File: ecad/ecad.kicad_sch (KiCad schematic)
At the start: 79 parts, among them J1 JTAG, J2 USB_C, SW1 Kailh choc v2, SW10 RotaryEncoder_Switch, SW11 RotaryEncoder_Switch, SW12 Kailh choc v2, SW13 Kailh choc v2, SW14 Kailh choc v2, SW15 RESET, SW16 Kailh choc v2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

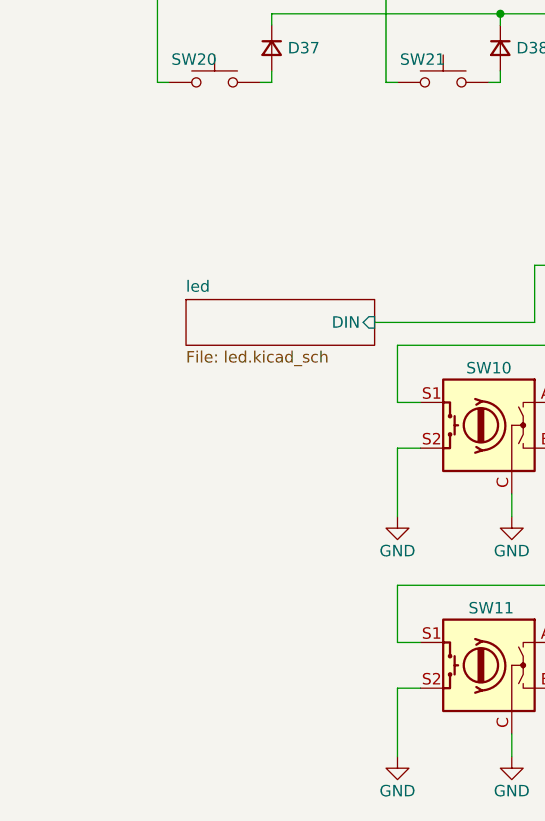
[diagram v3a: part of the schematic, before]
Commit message: feat(ecad): add buttons, fpc connector, and holes to pass flexible pcb of display
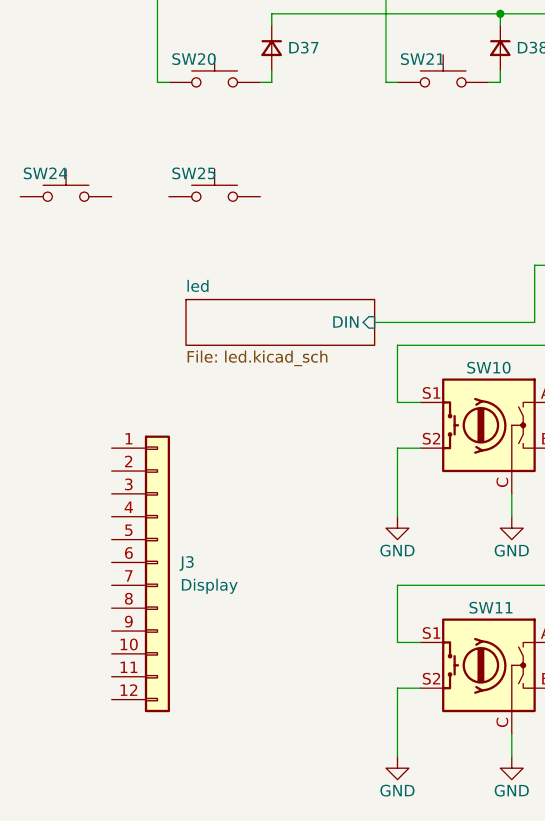
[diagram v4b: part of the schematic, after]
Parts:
- added J3: Display, Connector_FFC-FPC:Hirose_FH12-12S-0.5SH_1x12-1MP_P0.50mm_Horizontal, symbol Connector_Generic:Conn_01x12
- added SW24, SW25: Kailh choc v2, Button_Switch_THT:SW_PUSH_6mm, symbol Switch:SW_Push
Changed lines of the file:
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@@
+	)
+	(symbol
+		(lib_id "Switch:SW_Push")
+		(at 24.13 129.54 0)
+		(unit 1)
+		(exclude_from_sim no)
+		(in_bom yes)
+		(on_board yes)
+		(dnp no)
+		(property "Reference" "SW24"
+			(at 21.844 127 0)
+			(effects
+				(font
+					(size 1.27 1.27)
+				)
+			)
+		)
+		(property "Value" "Kailh choc v2"
+			(at 18.796 127 0)
+			(effects
+				(font
+					(size 1.27 1.27)
+				)
+				(hide yes)
+			)
+		)
+		(property "Footprint" "Button_Switch_THT:SW_PUSH_6mm"
+			(at 24.13 124.46 0)
+			(effects
+				(font
+					(size 1.27 1.27)
+				)
+				(hide yes)
+			)
+		)
+		(property "Datasheet" "~"
+			(at 24.13 124.46 0)
+			(effects
+				(font
+					(size 1.27 1.27)
+				)
+				(hide yes)
+			)
+		)
+		(property "Description" "Push button switch, generic, two pins"
+			(at 24.13 129.54 0)
+			(effects
+				(font
+					(size 1.27 1.27)
+				)
+				(hide yes)
+			)
+		)
+		(pin "1"
+		)
+		(pin "2"
+		)
+		(instances
+			(project "ecad"
+				(path "/c0f07fb6-3dcb-4a50-a8d5-ad7e01e28010"
+					(reference "SW24")
+					(unit 1)
+				)
+			)
+		)
 	)
 	(symbol
@@
 	)
 	(symbol
+		(lib_id "Switch:SW_Push")
+		(at 40.64 129.54 0)
+		(unit 1)
+		(exclude_from_sim no)
+		(in_bom yes)
+		(on_board yes)
+		(dnp no)
+		(property "Reference" "SW25"
+			(at 38.354 127 0)
+			(effects
+				(font
+					(size 1.27 1.27)
+				)
+			)
+		)
+		(property "Value" "Kailh choc v2"
+			(at 35.306 127 0)
+			(effects
+				(font
+					(size 1.27 1.27)
+				)
+				(hide yes)
+			)
+		)
+		(property "Footprint" "Button_Switch_THT:SW_PUSH_6mm"
+			(at 40.64 124.46 0)
+			(effects
+				(font
+					(size 1.27 1.27)
+				)
+				(hide yes)
+			)
+		)
+		(property "Datasheet" "~"
+			(at 40.64 124.46 0)
+			(effects
+				(font
+					(size 1.27 1.27)
+				)
+				(hide yes)
+			)
+		)
+		(property "Description" "Push button switch, generic, two pins"
+			(at 40.64 129.54 0)
+			(effects
+				(font
+					(size 1.27 1.27)
+				)
+				(hide yes)
+			)
+		)
+		(pin "1"
+		)
+		(pin "2"
+		)
+		(instances
+			(project "ecad"
+				(path "/c0f07fb6-3dcb-4a50-a8d5-ad7e01e28010"
+					(reference "SW25")
+					(unit 1)
+				)
+			)
+		)
+	)
+	(symbol
 		(lib_id "Device:C_Small")
 		(at 222.25 93.98 90)
@@
 					(unit 1)
 				)
+			)
+		)
+	)
+	(symbol
+		(lib_id "Connector_Generic:Conn_01x12")
+		(at 34.29 170.18 0)
+		(unit 1)
+		(exclude_from_sim no)
+		(in_bom yes)
+		(on_board yes)
+		(dnp no)
+		(fields_autoplaced yes)
+		(property "Reference" "J3"
+			(at 36.83 170.1799 0)
+			(effects
+				(font
+					(size 1.27 1.27)
+				)
+				(justify left)
+			)
+		)
+		(property "Value" "Display"
+			(at 36.83 172.7199 0)
+			(effects
+				(font
+					(size 1.27 1.27)
+				)
+				(justify left)
+			)
+		)
+		(property "Footprint" "Connector_FFC-FPC:Hirose_FH12-12S-0.5SH_1x12-1MP_P0.50mm_Horizontal"
+			(at 34.29 170.18 0)
+			(effects
+				(font
+					(size 1.27 1.27)
+				)
+				(hide yes)
+			)
+		)
+		(property "Datasheet" "~"
+			(at 34.29 170.18 0)
+			(effects
+				(font
+					(size 1.27 1.27)
+				)
+				(hide yes)
+			)
+		)
+		(property "Description" "Generic connector, single row, 01x12, script generated (kicad-library-utils/schlib/autogen/connector/)"
+			(at 34.29 170.18 0)
+			(effects
+				(font
+					(size 1.27 1.27)
+				)
+				(hide yes)
+			)
+		)
+		(pin "1"
+		)
+		(pin "2"
+		)
+		(pin "3"
+		)
+		(pin "4"
+		)
+		(pin "5"
+		)
+		(pin "6"
+		)
+		(pin "7"
+		)
+		(pin "8"
+		)
+		(pin "9"
+		)
+		(pin "10"
+		)
+		(pin "11"
+		)
+		(pin "12"
+		)
+		(instances
+			(project ""
+				(path "/c0f07fb6-3dcb-4a50-a8d5-ad7e01e28010"
+					(reference "J3")
+					(unit 1)
+				)

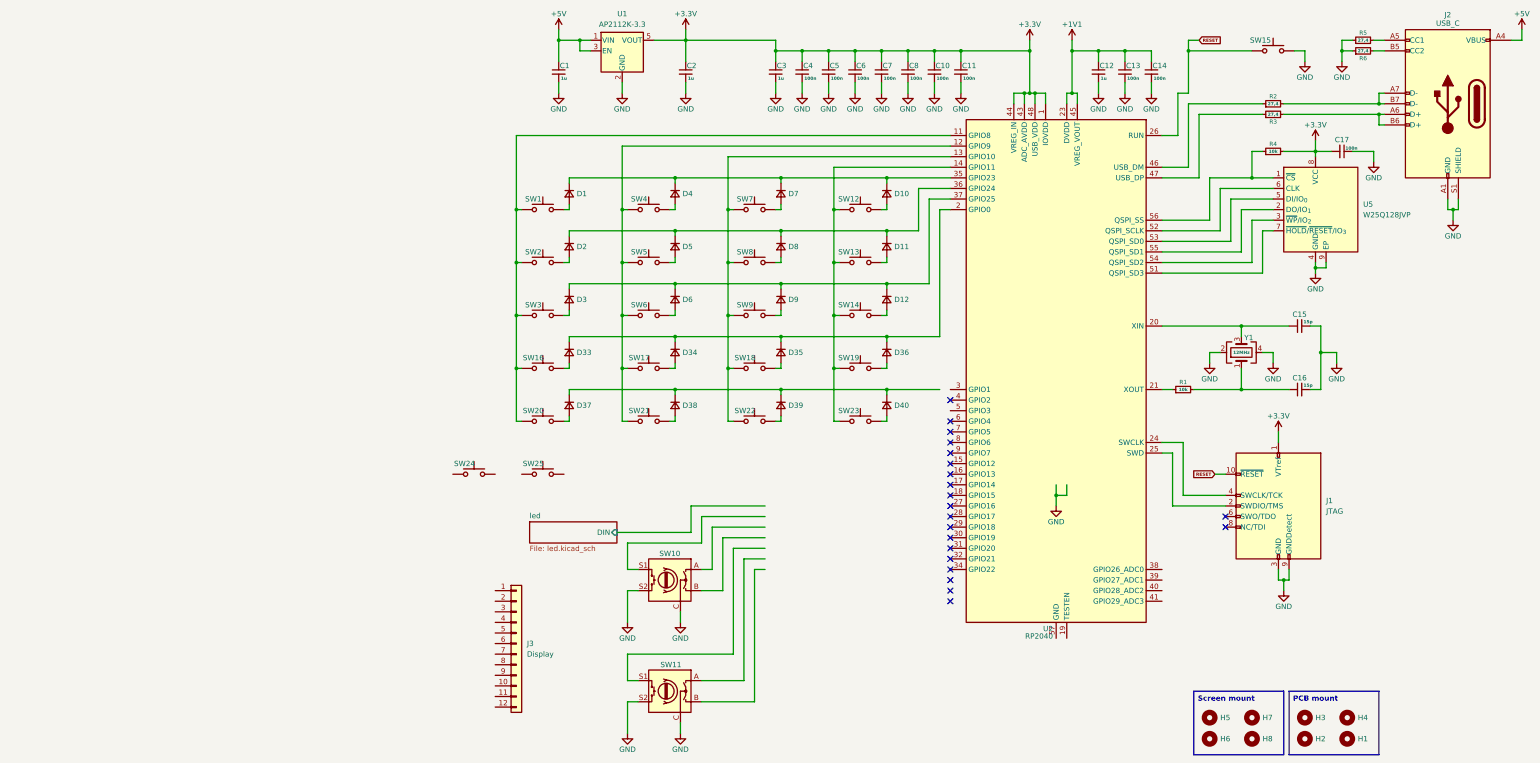
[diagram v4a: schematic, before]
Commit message: feat(ecad): hierarchical sheets, add switches net and change some components placement
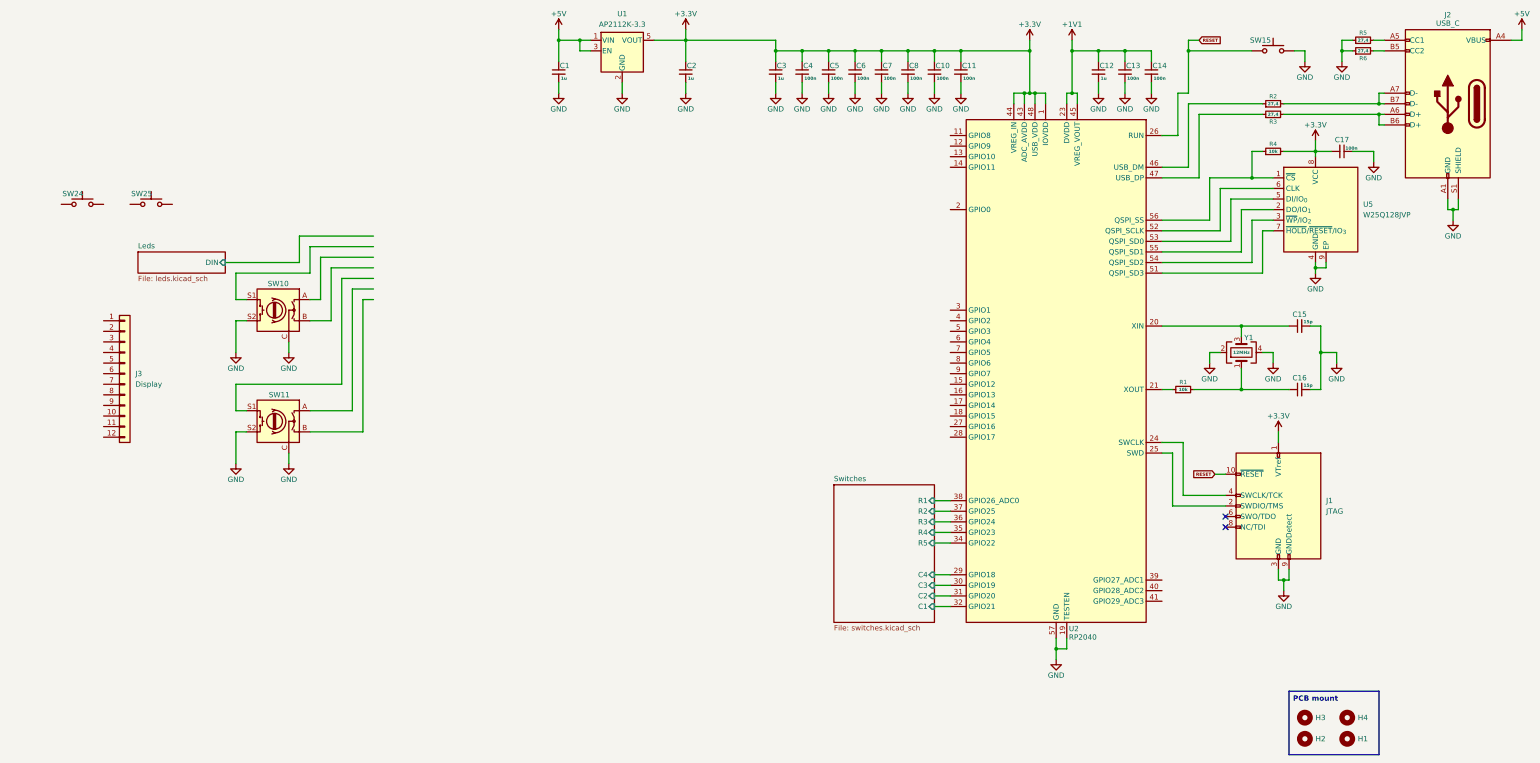
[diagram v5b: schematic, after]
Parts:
- removed D1, D10, D11, D12, D2, D3, D33, D34, D35, D36, D37, D38, D39, D4, D40, D5, D6, D7, D8, D9: D_Small, Diode_SMD:D_0402_1005Metric, symbol Device:D_Small
- removed H5, H6, H7, H8: MountingHole, MountingHole:MountingHole_2.2mm_M2_DIN965_Pad, symbol Mechanical:MountingHole
- removed SW1, SW12, SW13, SW14, SW16, SW17, SW18, SW19, SW2, SW20, SW21, SW22, SW23, SW3, SW4, SW5, SW6, SW7, SW8, SW9: Kailh choc v2, PCM_Switch_Keyboard_Hotswap_Kailh:SW_Hotswap_Kailh_Choc_V2, symbol Switch:SW_Push
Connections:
- net GND: now also U2.19 (TESTEN), U2.57 (GND)
- net Switches/R2: now reaches U2.37 (GPIO25)
- net Switches/R3: now reaches U2.36 (GPIO24)
- net Switches/R4: now reaches U2.35 (GPIO23)
- net Switches/C4: now reaches U2.29 (GPIO18)
- net Switches/C3: now reaches U2.30 (GPIO19)
- net Switches/C2: now reaches U2.31 (GPIO20)
- net Switches/C1: now reaches U2.32 (GPIO21)
- net Switches/R5: now reaches U2.34 (GPIO22)
- net Switches/R1: now reaches U2.38 (GPIO26_ADC0)
- no-connect marks 21 -> 2
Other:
- sheet led renamed Leds
- added sheet Switches (switches.kicad_sch)
- sheet Leds: file led.kicad_sch -> leds.kicad_sch
- moved on the sheet: J3, SW10, SW11, SW24, SW25

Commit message: feat(ecad): route rotary encoders and change some pins arrangement
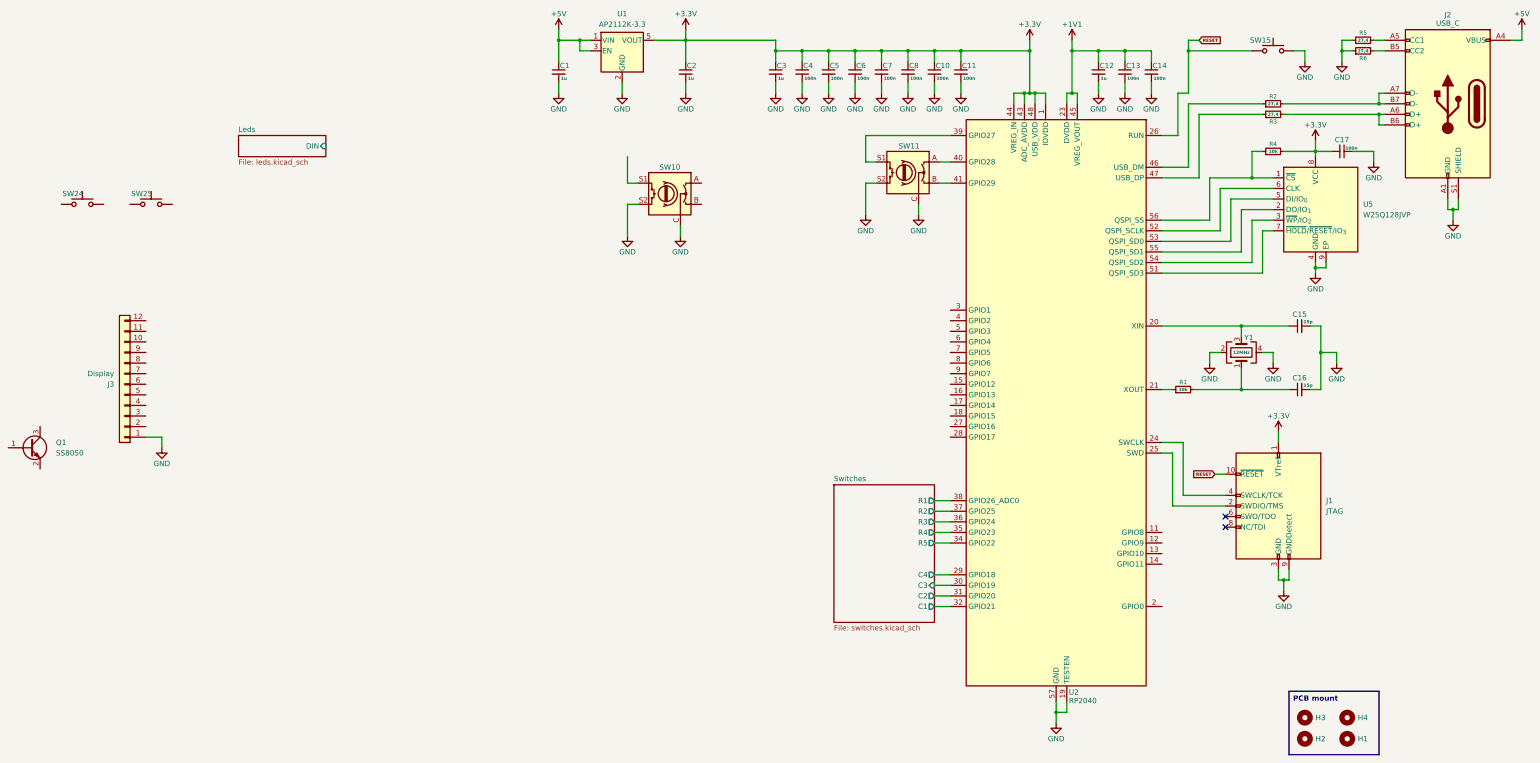
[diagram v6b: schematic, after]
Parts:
- added Q1: SS8050, Package_TO_SOT_SMD:SOT-23, symbol Transistor_BJT:SS8050
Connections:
- net GND: now also J3.1 (Pin_1)
- net at U2.39 (GPIO27): now also SW11.S1
- net at U2.40 (GPIO28): now also SW11.A
- net at U2.41 (GPIO29): now also SW11.B
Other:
- moved on the sheet: J3, SW10, SW11, U2

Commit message: feat(ecad): change ref of swtiche diode and make the circuitry for the display
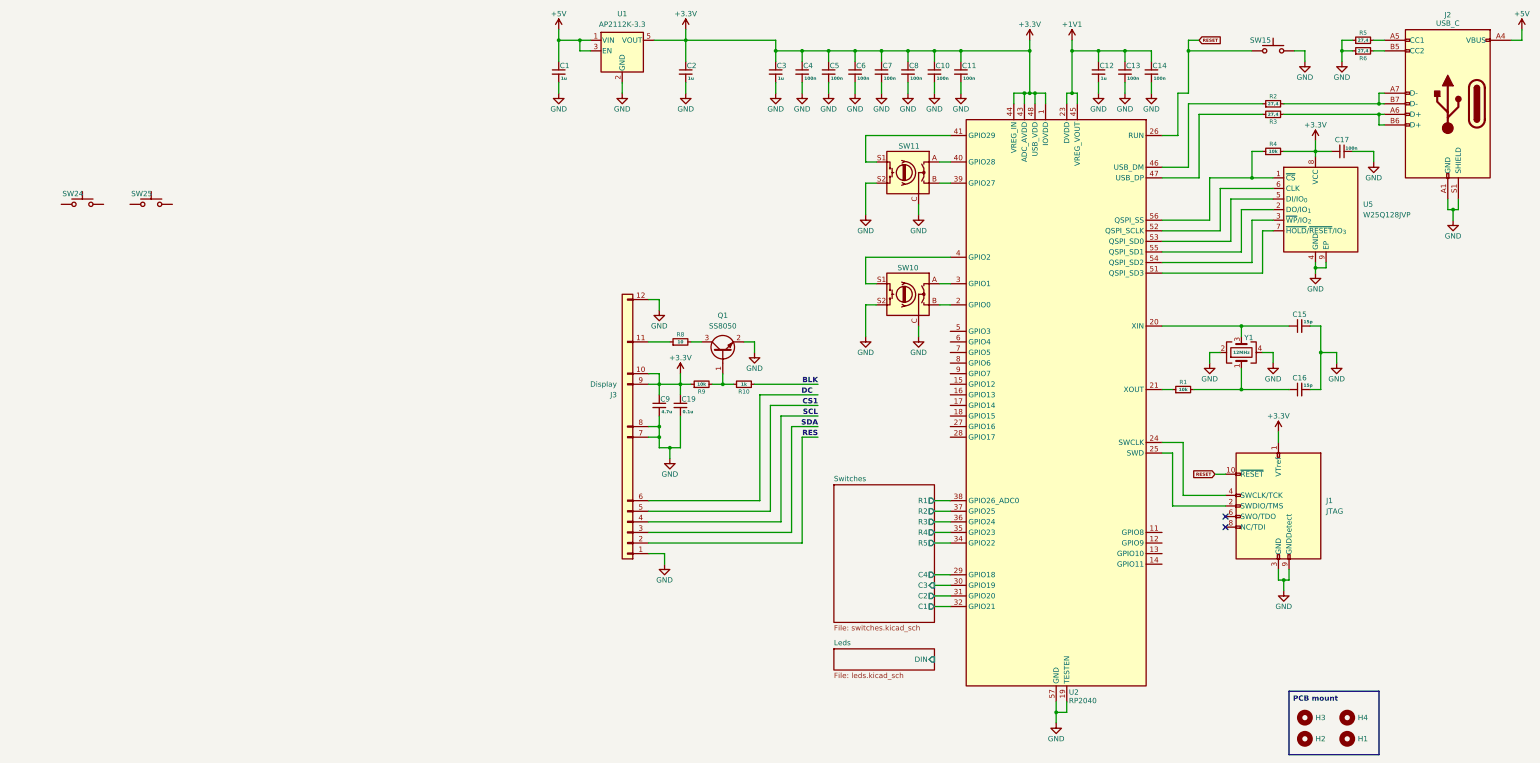
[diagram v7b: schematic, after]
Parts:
- added C19: 0.1u, Capacitor_SMD:C_0402_1005Metric, symbol Device:C_Small
- added C9: 4.7u, Capacitor_SMD:C_0402_1005Metric, symbol Device:C_Small
- added R10: 1k, Resistor_SMD:R_0402_1005Metric, symbol Device:R_Small
- added R8: 10, Resistor_SMD:R_0402_1005Metric, symbol Device:R_Small
- added R9: 10k, Resistor_SMD:R_0402_1005Metric, symbol Device:R_Small
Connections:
- net +3.3V: now also J3.10 (Pin_10), J3.9 (Pin_9), C19.1, C9.1, R9.1
- net GND: now also J3.12 (Pin_12), J3.7 (Pin_7), J3.8 (Pin_8), Q1.2 (E), C19.2, C9.2
- net at Q1.1 (B): now also R10.1, R9.2
- net at Q1.3 (C): now also R8.2
- net at J3.11 (Pin_11): now also R8.1
- net RES: now reaches J3.2 (Pin_2)
- net SDA: now reaches J3.3 (Pin_3)
- net SCL: now reaches J3.4 (Pin_4)
- net CS1: now reaches J3.5 (Pin_5)
- net DC: now reaches J3.6 (Pin_6)
- net at U2.2 (GPIO0): now also SW10.B
- net at U2.3 (GPIO1): now also SW10.A
- net at U2.39 (GPIO27): now also SW11.B; no longer SW11.S1
- net at U2.4 (GPIO2): now also SW10.S1
- net at U2.41 (GPIO29): now also SW11.S1; no longer SW11.B
- new net BLK: R10.2
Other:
- moved on the sheet: J3, Q1, SW10

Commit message: feat(ecad): general routing
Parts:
- removed Q1: SS8050, Package_TO_SOT_SMD:SOT-23, symbol Transistor_BJT:SS8050
- removed R10: 1k, Resistor_SMD:R_0402_1005Metric, symbol Device:R_Small
- removed R8: 10, Resistor_SMD:R_0402_1005Metric, symbol Device:R_Small
- removed R9: 10k, Resistor_SMD:R_0402_1005Metric, symbol Device:R_Small
- added H5, H6, H7, H8: MountingHole, MountingHole:MountingHole_2.2mm_M2_DIN965, symbol Mechanical:MountingHole
- added Q2: SS8050, Package_TO_SOT_SMD:SOT-23, symbol Transistor_BJT:SS8050
- added R11: 10, Resistor_SMD:R_0402_1005Metric, symbol Device:R_Small
- added R12: 1k, Resistor_SMD:R_0402_1005Metric, symbol Device:R_Small
- added R13: 10k, Resistor_SMD:R_0402_1005Metric, symbol Device:R_Small
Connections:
- net CS1 is gone; now on net +3.3V: J3.5 (Pin_5)
- net +3.3V: now also J3.3 (Pin_3), J3.4 (Pin_4), R13.1; no longer J3.10 (Pin_10), J3.9 (Pin_9)
- net BLK: now also U2.15 (GPIO12), R12.2
- net DC: now also J3.10 (Pin_10), U2.17 (GPIO14); no longer J3.6 (Pin_6)
- net GND: now also SW24.2, SW25.2, Q2.2 (E); no longer J3.7 (Pin_7), J3.8 (Pin_8)
- net Leds/DIN: now also U2.5 (GPIO3)
- net RES: now also J3.7 (Pin_7), U2.16 (GPIO13); no longer J3.2 (Pin_2)
- net SCL: now also J3.9 (Pin_9), U2.13 (GPIO10); no longer J3.4 (Pin_4)
- net SDA: now also J3.8 (Pin_8), U2.14 (GPIO11); no longer J3.3 (Pin_3)
- net CS: now reaches J3.11 (Pin_11)
- net CS: now also U2.12 (GPIO9)
- net at SW24.1: now also U2.27 (GPIO16)
- net at SW25.1: now also U2.28 (GPIO17)
- new net: Q2.1 (B), R12.1, R13.2
- new net: Q2.3 (C), R11.2
- new net LEDK: J3.2 (Pin_2), R11.1
- no-connect marks 2 -> 9
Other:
- moved on the sheet: C19, C9, H1, H2, H3, H4, J3, SW24, SW25
